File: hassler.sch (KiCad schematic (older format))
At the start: 33 parts

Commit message: Minor corrections to schematic
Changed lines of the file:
@@
 $Descr A4 11693 8268
 encoding utf-8
-Sheet 1 2
+Sheet 1 3
 Title "Portable Hassler circuit"
 Date "Mon 02 Feb 2015"
@@
 	6350 4950 6350 2850
 $Sheet
-S 2300 5200 950  750
+S 2300 5200 1200 750
 U 54D134FA
 F0 "LithiumUSBPower" 60
 F1 "lipo-usb-power.sch" 60
 $EndSheet
+$Sheet
+S 3850 5200 1250 750
+U 54D1590C
+F0 "LithiumBoostTo10V" 60
+F1 "lipo-boost-10v.sch" 60
+$EndSheet
 $EndSCHEMATC

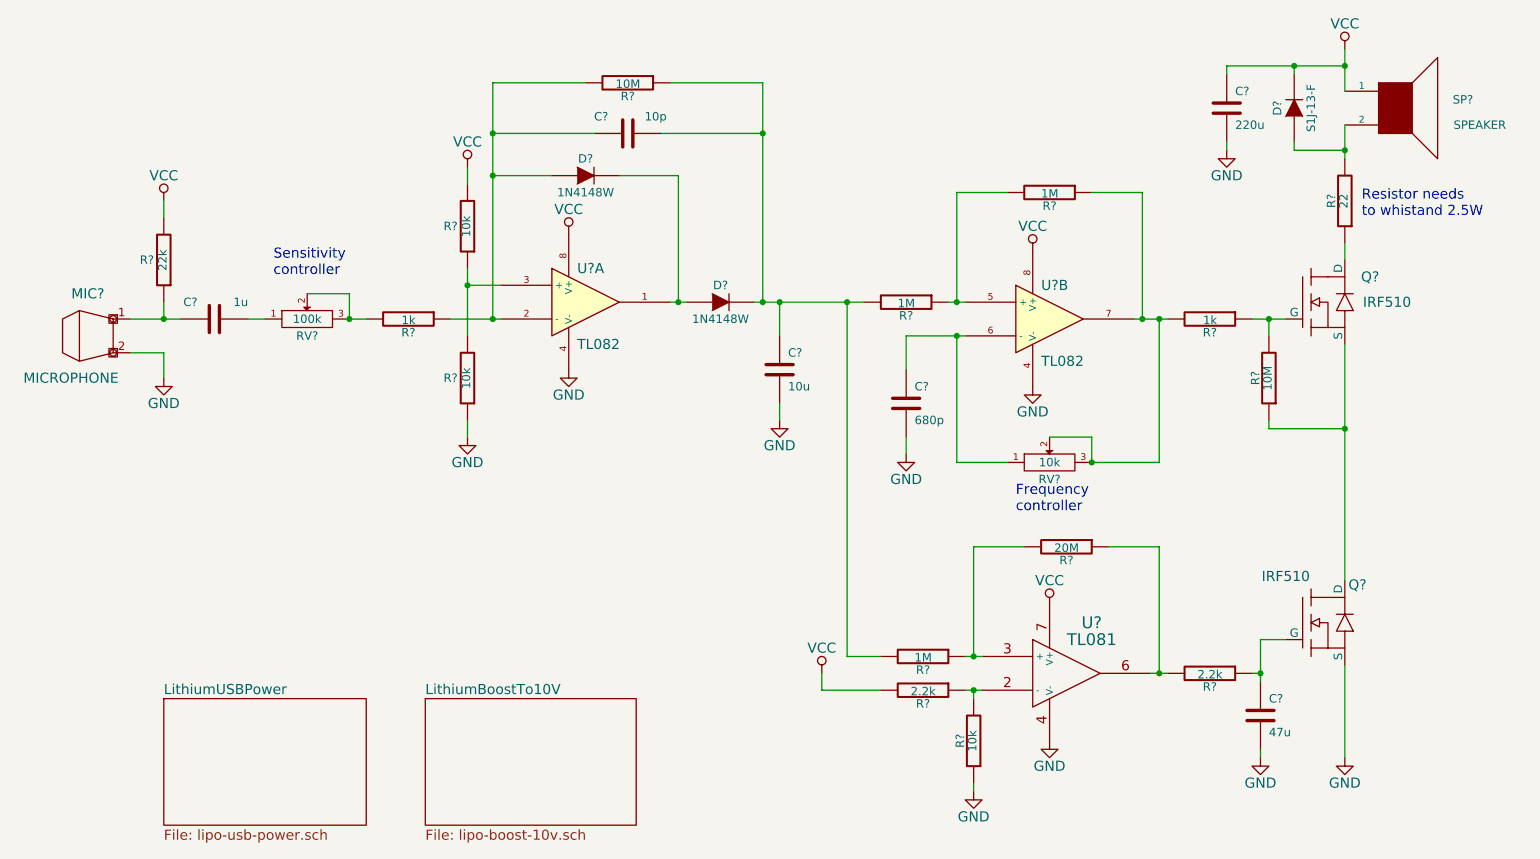
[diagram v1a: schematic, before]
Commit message: Add low-battery detection stage
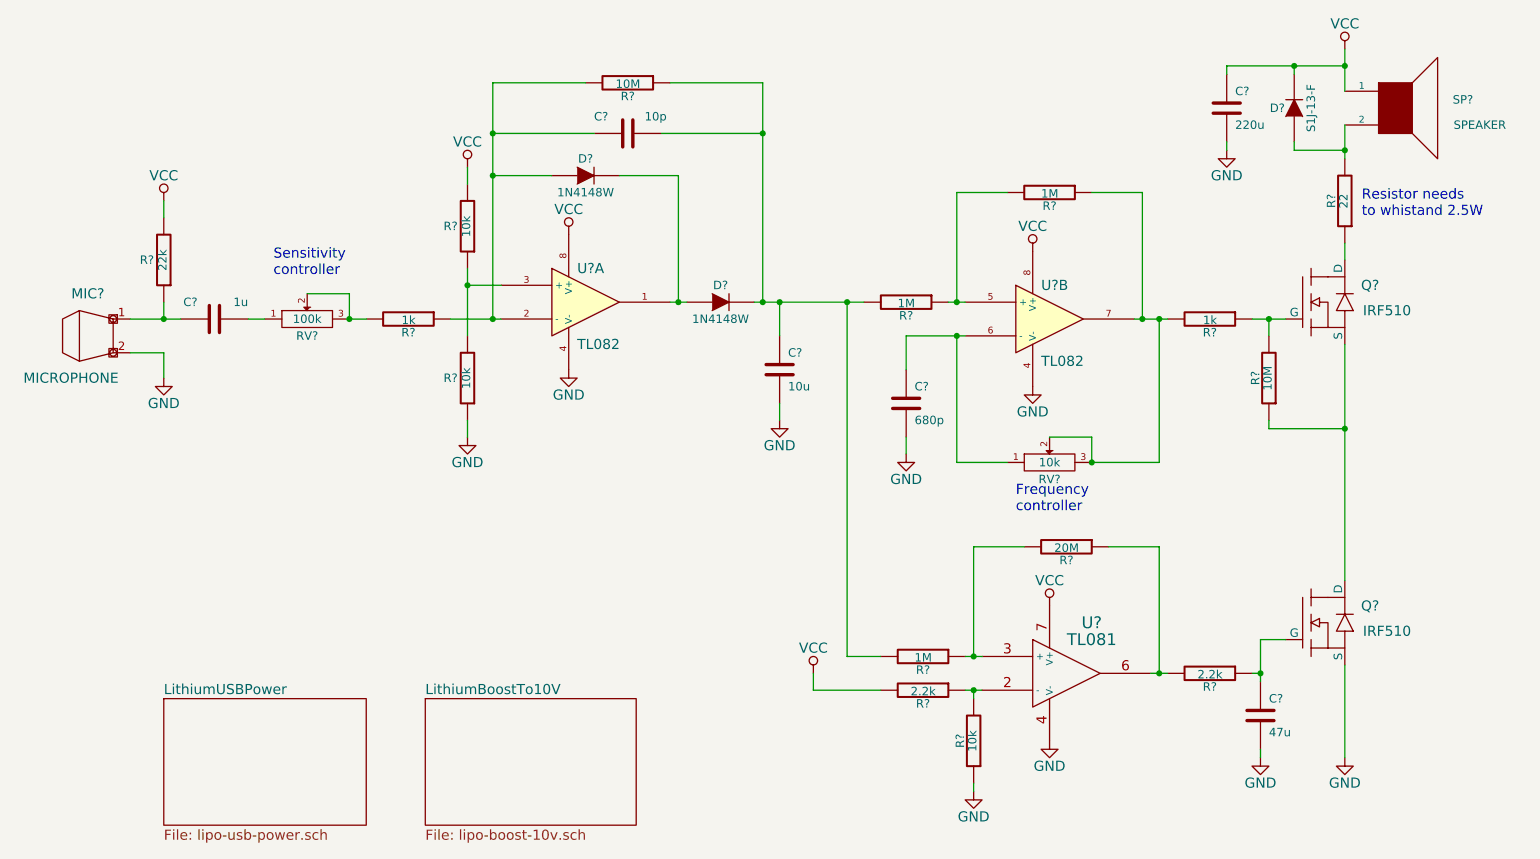
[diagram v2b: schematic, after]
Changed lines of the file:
@@
 U 1 1 54D00111
 P 9000 1700
-F 0 "D?" H 9000 1800 50  0000 C CNN
+F 0 "D?" V 9000 1800 50  0000 C CNN
 F 1 "S1J-13-F" H 9000 1600 50  0000 C CNN
 F 2 "" H 9000 1700 60  0000 C CNN
@@
 U 1 1 54D00EE5
 P 9200 2850
-F 0 "Q?" H 9450 3000 60  0000 C CNN
-F 1 "IRF510" H 9550 2850 60  0000 C CNN
+F 0 "Q?" H 9450 2950 60  0000 C CNN
+F 1 "IRF510" H 9550 2800 60  0000 C CNN
 F 2 "" H 9200 2850 60  0000 C CNN
 F 3 "" H 9200 2850 60  0000 C CNN
@@
 U 1 1 54D01029
 P 9200 4750
-F 0 "Q?" H 9375 4975 60  0000 C CNN
-F 1 "IRF510" H 8950 5025 60  0000 C CNN
+F 0 "Q?" H 9450 4850 60  0000 C CNN
+F 1 "IRF510" H 9550 4700 60  0000 C CNN
 F 2 "" H 9200 4750 60  0000 C CNN
 F 3 "" H 9200 4750 60  0000 C CNN
@@
 	2300 3150 2100 3150
 Wire Wire Line
-	2100 2950 2400 2950
+	2100 2950 2300 2950
+Wire Wire Line
+	2300 2950 2400 2950
 Wire Wire Line
 	2300 2950 2300 2850
@@
 Connection ~ 3400 2950
 Wire Wire Line
-	4100 2650 4100 3050
-Wire Wire Line
-	4000 2950 4300 2950
+	4100 2650 4100 2750
+Wire Wire Line
+	4100 2750 4100 3050
+Wire Wire Line
+	4000 2950 4250 2950
+Wire Wire Line
+	4250 2950 4300 2950
 Wire Wire Line
 	4300 2750 4100 2750
@@
 	4250 2100 4600 2100
 Wire Wire Line
-	4250 1550 4250 2950
+	4250 1550 4250 1850
+Wire Wire Line
+	4250 1850 4250 2100
+Wire Wire Line
+	4250 2100 4250 2950
 Connection ~ 4250 2950
 Wire Wire Line
@@
 	5350 2100 5350 2850
 Wire Wire Line
-	5300 2850 5400 2850
+	5300 2850 5350 2850
+Wire Wire Line
+	5350 2850 5400 2850
 Connection ~ 5350 2850
 Wire Wire Line
-	5800 2850 6450 2850
+	5800 2850 5850 2850
+Wire Wire Line
+	5850 2850 5950 2850
+Wire Wire Line
+	5950 2850 6350 2850
+Wire Wire Line
+	6350 2850 6450 2850
 Wire Wire Line
 	5300 1550 5850 1550
@@
 	5950 3450 5950 3550
 Wire Wire Line
-	5850 1550 5850 2850
+	5850 1550 5850 1850
+Wire Wire Line
+	5850 1850 5850 2850
 Wire Wire Line
 	5250 1850 5850 1850
@@
 $EndComp
 Wire Wire Line
-	6700 3050 7050 3050
+	6700 3050 7000 3050
+Wire Wire Line
+	7000 3050 7050 3050
 Wire Wire Line
 	7000 3050 7000 3800
@@
 	8200 3800 8200 2950
 Wire Wire Line
-	8050 2950 8250 2950
+	8050 2950 8100 2950
+Wire Wire Line
+	8100 2950 8200 2950
+Wire Wire Line
+	8200 2950 8250 2950
 Connection ~ 7000 3050
 $Comp
@@
 	8850 3050 8850 2950
 Wire Wire Line
-	8750 2950 8950 2950
+	8750 2950 8850 2950
+Wire Wire Line
+	8850 2950 8950 2950
 Connection ~ 8850 2950
 Wire Wire Line
@@
 	8850 3600 9300 3600
 Wire Wire Line
-	9300 3100 9300 4500
+	9300 3100 9300 3600
+Wire Wire Line
+	9300 3600 9300 4500
 Wire Wire Line
 	9300 2500 9300 2600
 Wire Wire Line
-	9300 1800 9300 2000
+	9300 1800 9300 1950
+Wire Wire Line
+	9300 1950 9300 2000
 Wire Wire Line
 	9000 1900 9000 1950
@@
 Connection ~ 9300 1950
 Wire Wire Line
-	9300 1350 9300 1600
-Wire Wire Line
-	8600 1450 9300 1450
+	9300 1350 9300 1450
+Wire Wire Line
+	9300 1450 9300 1600
+Wire Wire Line
+	8600 1450 9000 1450
+Wire Wire Line
+	9000 1450 9300 1450
 Wire Wire Line
 	9000 1450 9000 1500
@@
 	7100 4300 7100 4950
 Wire Wire Line
-	7050 4950 7150 4950
+	7050 4950 7100 4950
+Wire Wire Line
+	7100 4950 7150 4950
 Connection ~ 7100 4950
 Wire Wire Line
-	7050 5150 7150 5150
+	7050 5150 7100 5150
+Wire Wire Line
+	7100 5150 7150 5150
 $Comp
 L R R?
@@
 L VCC #PWR?
 U 1 1 54D0CD64
-P 6200 5050
-F 0 "#PWR?" H 6200 4900 60  0001 C CNN
-F 1 "VCC" H 6200 5200 60  0000 C CNN
-F 2 "" H 6200 5050 60  0000 C CNN
-F 3 "" H 6200 5050 60  0000 C CNN
-	1    6200 5050
-	1    0    0    -1
-$EndComp
-Wire Wire Line
-	6200 5050 6200 5150
-Wire Wire Line
-	6200 5150 6550 5150
+P 6150 5050
+F 0 "#PWR?" H 6150 4900 60  0001 C CNN
+F 1 "VCC" H 6150 5200 60  0000 C CNN
+F 2 "" H 6150 5050 60  0000 C CNN
+F 3 "" H 6150 5050 60  0000 C CNN
+	1    6150 5050
+	1    0    0    -1
+$EndComp
+Wire Wire Line
+	6150 5050 6150 5150
+Wire Wire Line
+	6150 5150 6550 5150
 Wire Wire Line
 	6550 4950 6350 4950
 Connection ~ 6350 2850
 Wire Wire Line
-	8150 5050 8250 5050
+	8150 5050 8200 5050
+Wire Wire Line
+	8200 5050 8250 5050
 Wire Wire Line
 	8200 5050 8200 4300
@@
 	8800 5550 8800 5500
 Wire Wire Line
-	8800 4850 8800 5100
+	8800 4850 8800 5050
+Wire Wire Line
+	8800 5050 8800 5100
 Wire Wire Line
 	8800 5050 8750 5050
@@
 	6700 3050 6700 3250
 Wire Wire Line
-	6950 2850 7050 2850
+	6950 2850 7000 2850
+Wire Wire Line
+	7000 2850 7050 2850
 Wire Wire Line
 	8100 2200 8100 2950

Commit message: Correct value of a resistor & Generate netlist
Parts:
- gave numbers to parts that had none: 32

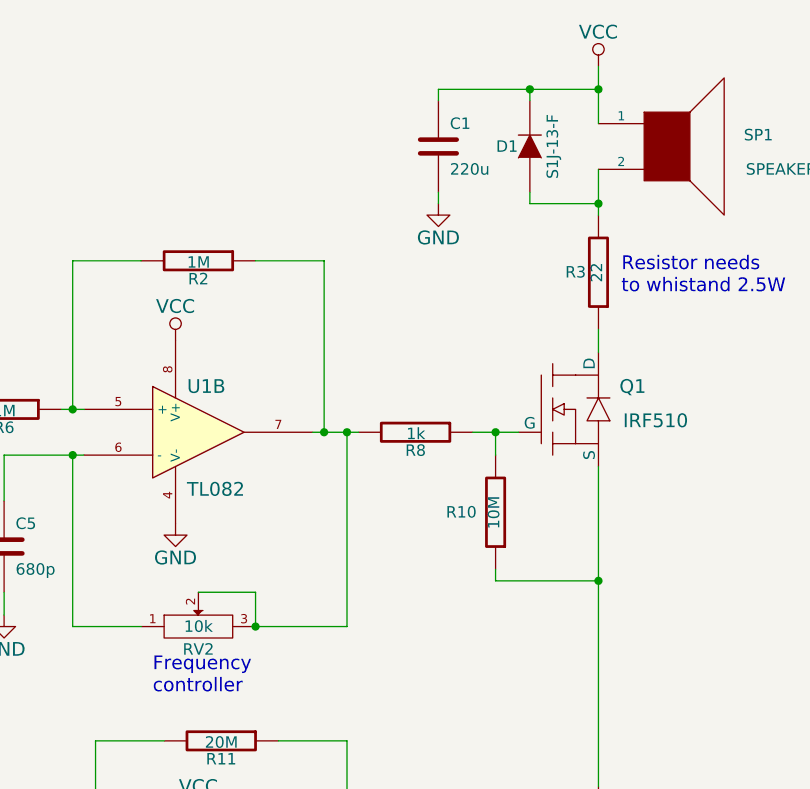
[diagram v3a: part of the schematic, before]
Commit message: Associate footprints to components
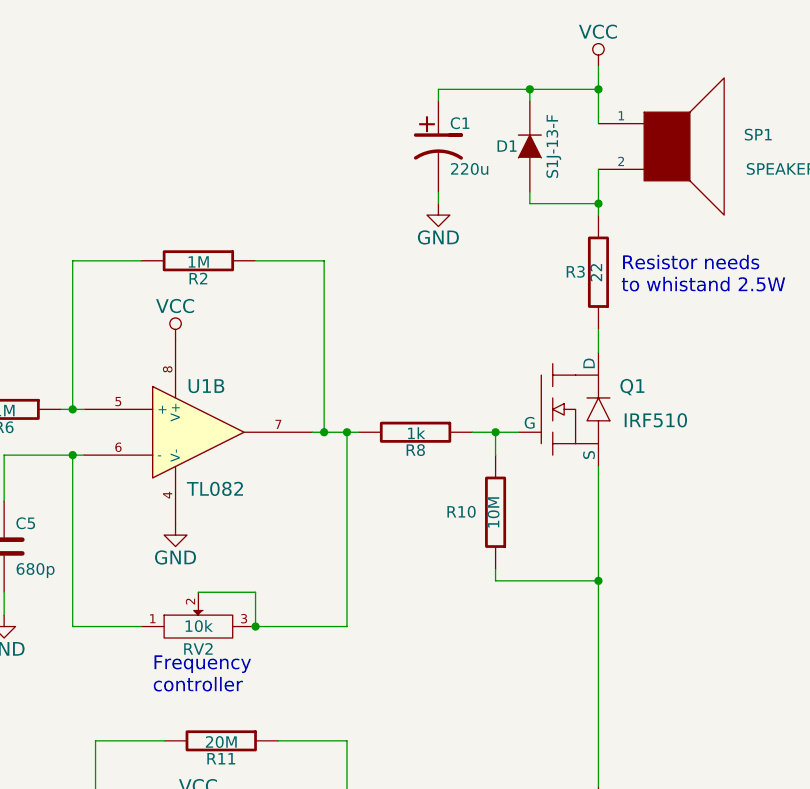
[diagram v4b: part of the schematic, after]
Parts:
- removed C1: 220u, symbol C
- added C1: 220u, symbol CP1
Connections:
- net GND: now also C1.2
- net VCC: now also C1.1
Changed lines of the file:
@@
 	0    -1   -1   0
-$EndComp
-$Comp
-L C C1
-U 1 1 54D0019F
-P 8600 1700
-F 0 "C1" H 8650 1800 50  0000 L CNN
-F 1 "220u" H 8650 1600 50  0000 L CNN
-F 2 "" H 8638 1550 30  0000 C CNN
-F 3 "" H 8600 1700 60  0000 C CNN
-	1    8600 1700
-	1    0    0    -1
 $EndComp
 Text Notes 9400 2350 0    60   ~ 0
@@
 	7800 3800 8200 3800
 Wire Wire Line
-	8200 2950 8200 3800
+	8200 3800 8200 2950
 Wire Wire Line
 	8050 2950 8250 2950
@@
 Wire Wire Line
 	8800 5500 8800 5550
+$Comp
+L CP1 C1
+U 1 1 54D2FE33
+P 8600 1700
+F 0 "C1" H 8650 1800 50  0000 L CNN
+F 1 "220u" H 8650 1600 50  0000 L CNN
+F 2 "" H 8600 1700 60  0000 C CNN
+F 3 "" H 8600 1700 60  0000 C CNN
+	1    8600 1700
+	1    0    0    -1
+$EndComp
 $EndSCHEMATC
